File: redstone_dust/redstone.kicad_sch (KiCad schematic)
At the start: 72 parts, among them J1 1x4_Pogo, J2 1x4_Pogo, J3 1x4_Pogo, J4 1x4_Pogo, J5 1x4_Pogo, J6 1x4_Pogo, J7 1x4_Pogo, J8 1x4_Pogo, J9 2.54mm_ProgrammingPin, Q1 BC108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

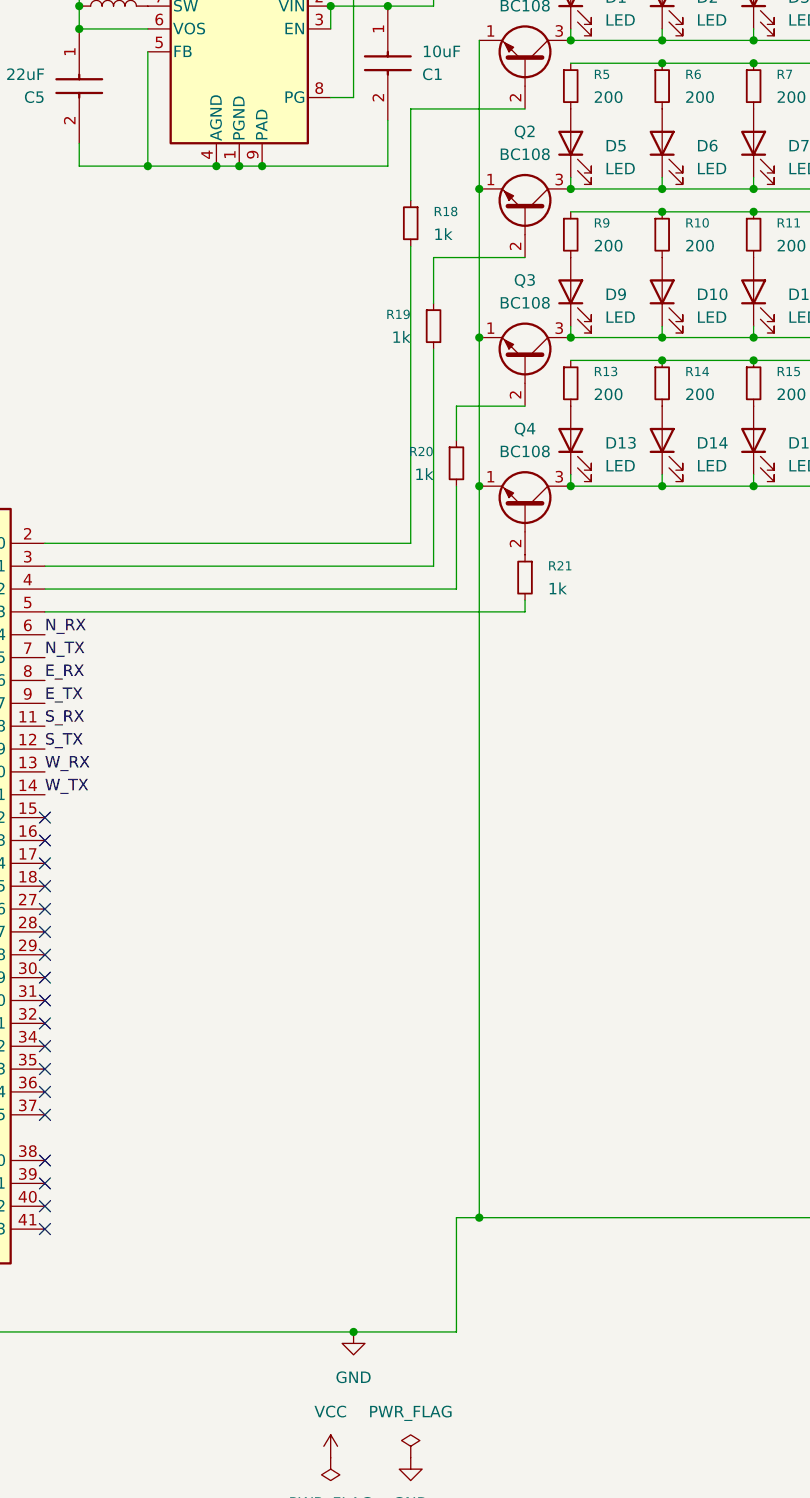
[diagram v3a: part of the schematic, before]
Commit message: add basic pcb layout, fix disconnected ground net
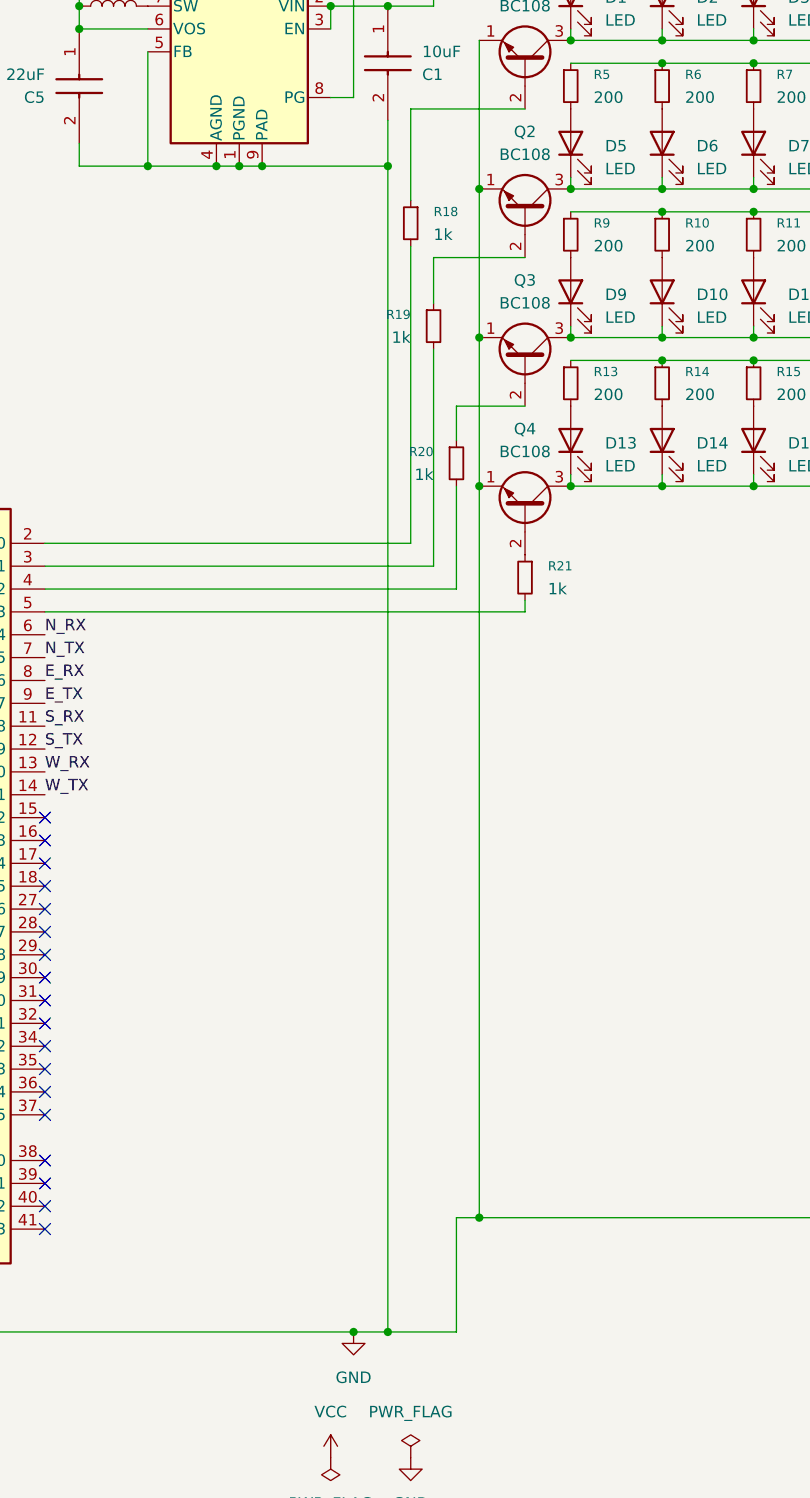
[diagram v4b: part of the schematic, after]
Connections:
- net GND: now also C1.2, C5.2, U3.1 (PGND), U3.4 (AGND), U3.5 (FB), U3.9 (PAD)
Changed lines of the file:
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@@
+	)
+	(junction
+		(at 166.37 173.99)
+		(diameter 0)
+		(color 0 0 0 1)
 	)
 	(junction
@@
 	)
 	(junction
+		(at 166.37 44.45)
+		(diameter 0)
+		(color 0 0 0 1)
+	)
+	(junction
 		(at 110.49 16.51)
 		(diameter 0)
@@
 	(wire
 		(pts
+			(xy 166.37 173.99) (xy 173.99 173.99)
+		)
+		(stroke
+			(width 0)
+			(type default)
+			(color 0 0 0 1)
+		)
+	)
+	(wire
+		(pts
 			(xy 48.26 149.86) (xy 48.26 86.36)
 		)
@@
 	(wire
 		(pts
+			(xy 166.37 44.45) (xy 166.37 173.99)
+		)
+		(stroke
+			(width 0)
+			(type default)
+			(color 0 0 0 1)
+		)
+	)
+	(wire
+		(pts
 			(xy 82.55 59.69) (xy 82.55 67.31)
 		)
@@
 	(wire
 		(pts
-			(xy 162.56 173.99) (xy 173.99 173.99)
-		)
-		(stroke
+			(xy 162.56 173.99) (xy 166.37 173.99)
+		)
+		(stroke

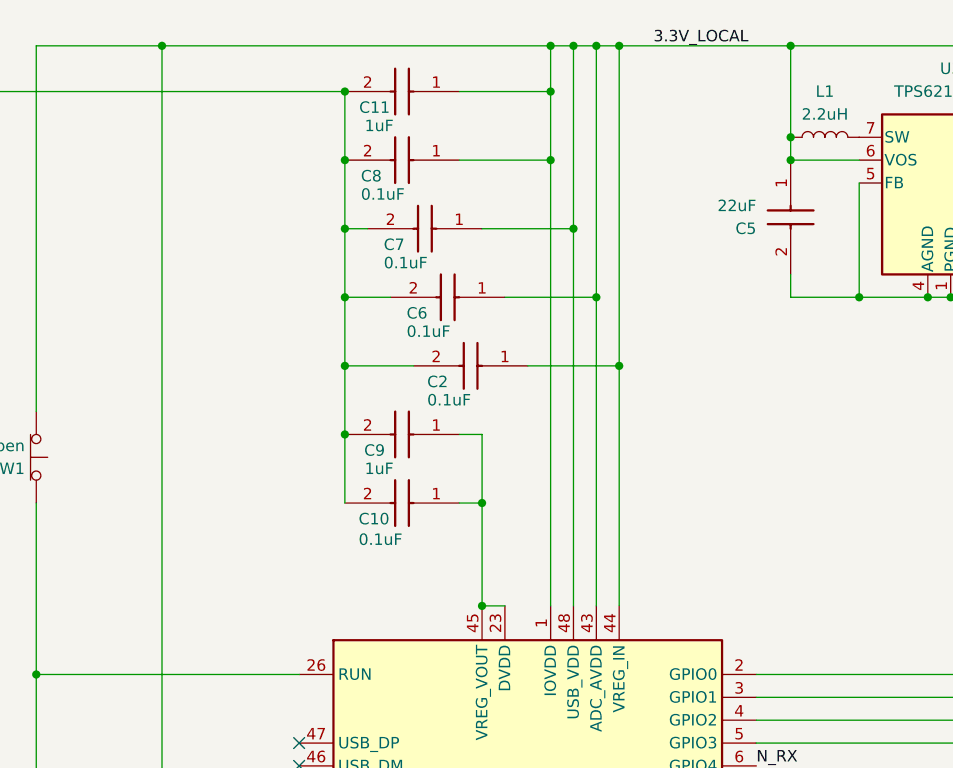
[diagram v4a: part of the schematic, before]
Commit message: remove some unecessary capacitors
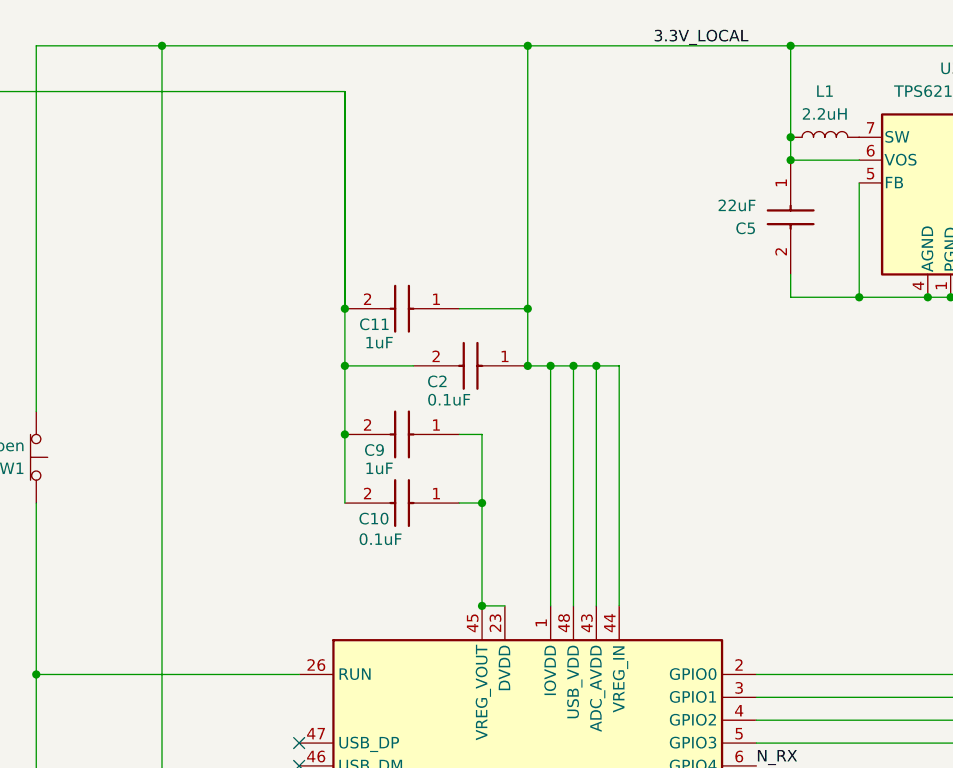
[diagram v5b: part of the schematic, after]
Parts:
- removed C6, C7, C8: 0.1uF, CAPC2012X140N, symbol SamacSys_Parts:C0805F104K1RACAUTO
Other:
- moved on the sheet: C11

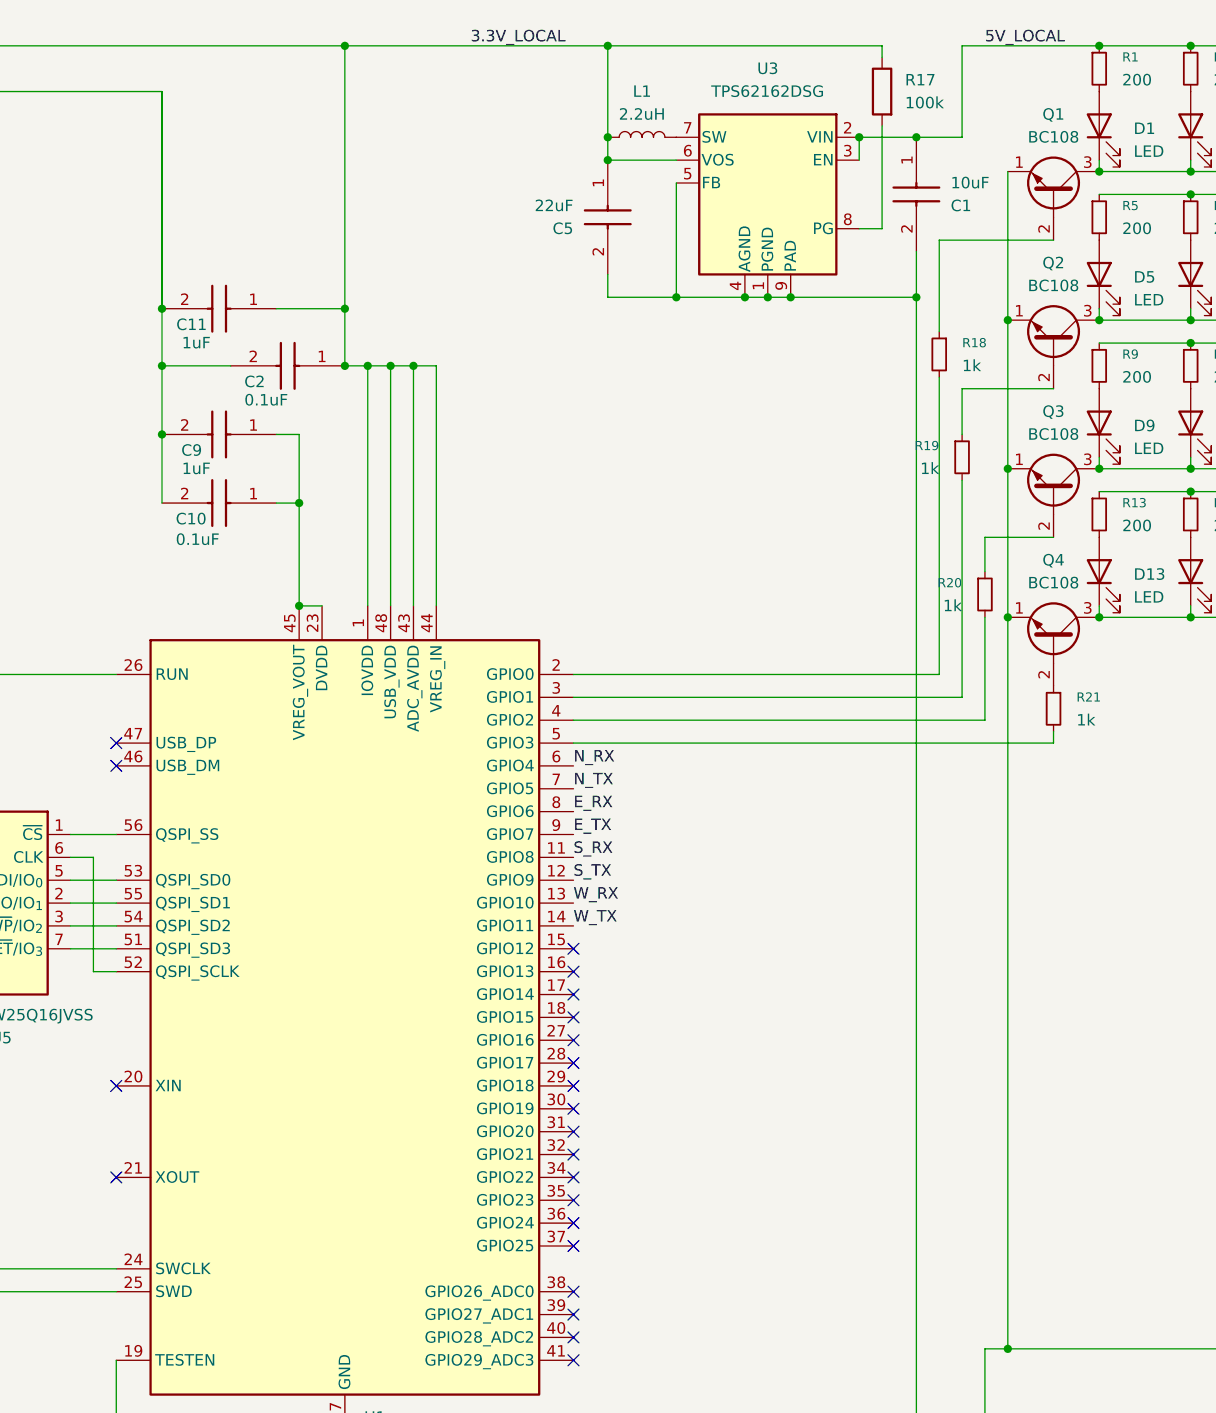
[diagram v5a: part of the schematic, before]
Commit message: redoing pcb layout with new approach
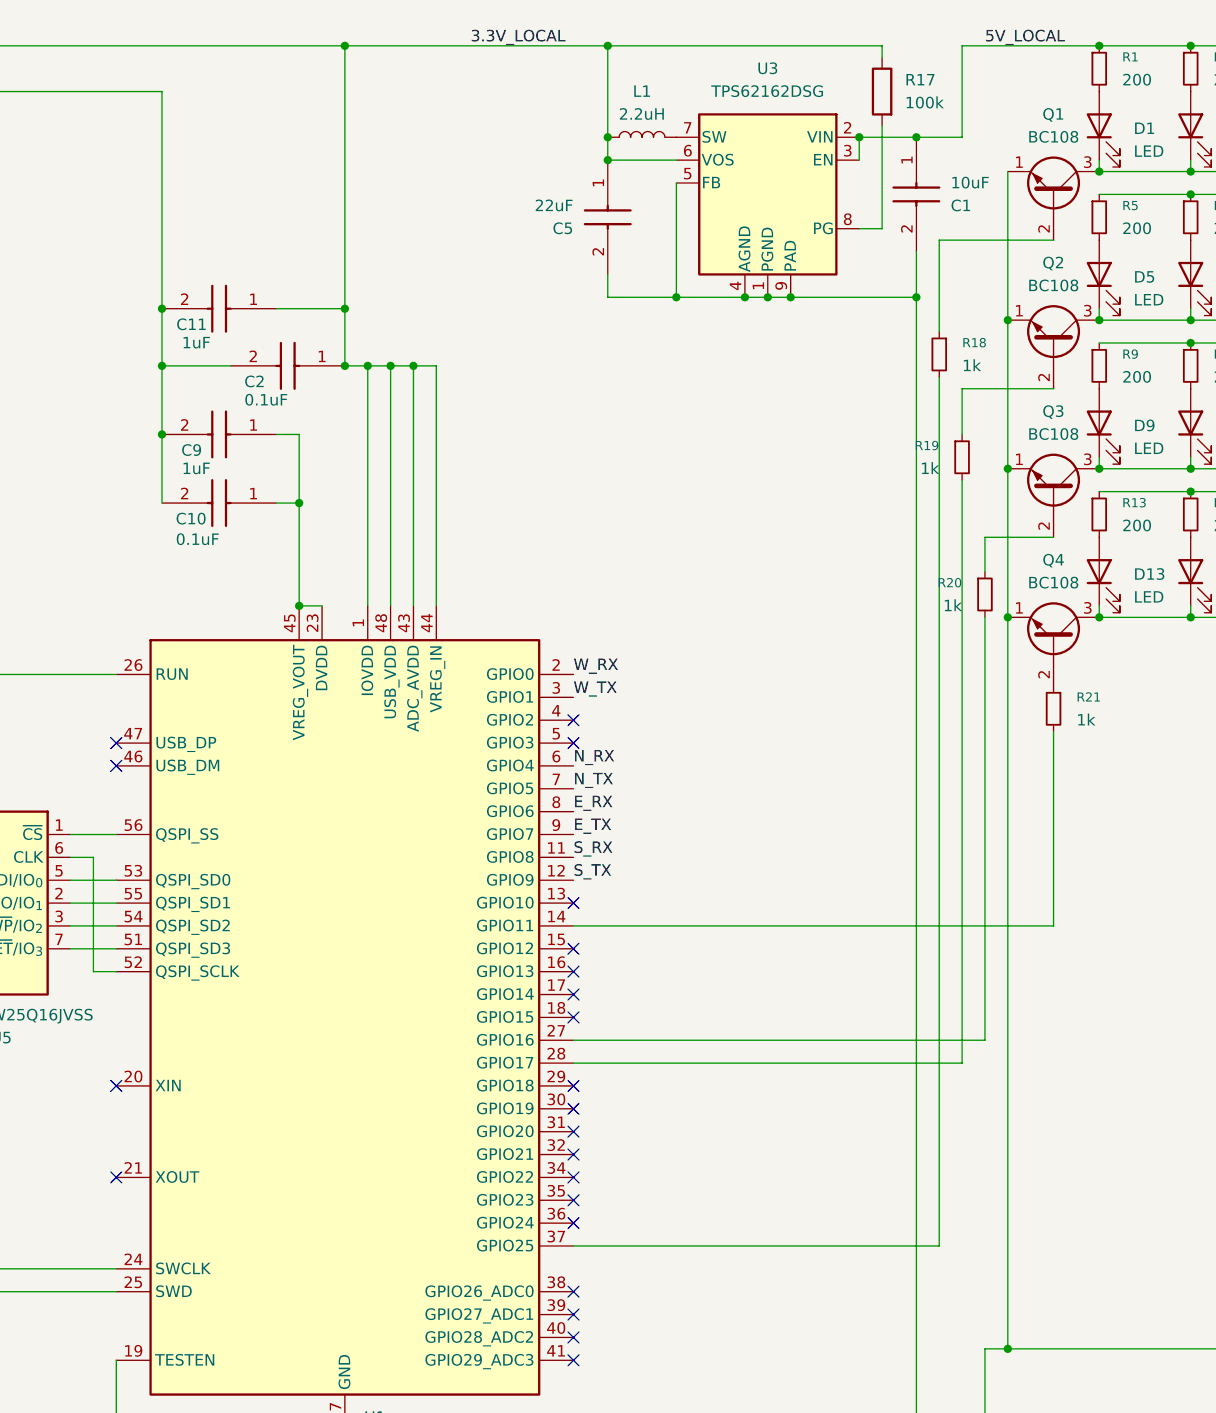
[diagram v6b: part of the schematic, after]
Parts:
- C1: footprint CAPC1005X70N -> SamacSys_Parts:CAPC1005X70N
- C10, C2, C3: footprint CAPC2012X140N -> SamacSys_Parts:CAPC2012X140N
- C11, C9: footprint CAPC0603X33N -> SamacSys_Parts:CAPC0603X33N
- C4, C5: footprint GRM18x -> SamacSys_Parts:GRM18x
- D17, D18, D20, D21: footprint SOT95P248X115-3N -> SamacSys_Parts:SOT95P248X115-3N
- D19: footprint DIOM5436X244N -> SamacSys_Parts:DIOM5436X244N
- U2: footprint RBT10W24S05_XPP_XPR -> SamacSys_Parts:RBT10W24S05_XPP_XPR
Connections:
- net W_RX: now also U1.2 (GPIO0); no longer U1.13 (GPIO10)
- net W_TX: now also U1.3 (GPIO1); no longer U1.14 (GPIO11)
- net at R18.2: now also U1.37 (GPIO25); no longer U1.2 (GPIO0)
- net at R19.2: now also U1.28 (GPIO17); no longer U1.3 (GPIO1)
- net at R20.2: now also U1.27 (GPIO16); no longer U1.4 (GPIO2)
- net at R21.2: now also U1.14 (GPIO11); no longer U1.5 (GPIO3)
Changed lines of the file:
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@@
 	)
 	(no_connect
-		(at 128.27 129.54)
+		(at 128.27 93.98)
 	)
 	(no_connect
@@
 	)
 	(no_connect
-		(at 128.27 149.86)
+		(at 128.27 111.76)
 	)
 	(no_connect
@@
 	)
 	(no_connect
-		(at 128.27 127)
+		(at 128.27 91.44)
 	)
 	(no_connect
@@
 	(wire
 		(pts
-			(xy 171.45 88.9) (xy 171.45 64.77)
+			(xy 171.45 64.77) (xy 171.45 129.54)
 		)
 		(stroke
@@
 	(wire
 		(pts
-			(xy 128.27 93.98) (xy 181.61 93.98)
+			(xy 128.27 114.3) (xy 181.61 114.3)
 		)
 		(stroke
@@
 	(wire
 		(pts
-			(xy 168.91 53.34) (xy 168.91 86.36)
-		)
-		(stroke
-			(width 0)
-			(type default)
-			(color 0 194 194 1)
-		)
-	)
-	(wire
-		(pts
 			(xy 257.81 59.69) (xy 265.43 59.69)
 		)
@@
 	(wire
 		(pts
-			(xy 128.27 91.44) (xy 173.99 91.44)
+			(xy 128.27 127) (xy 173.99 127)
 		)
 		(stroke
@@
 	(wire
 		(pts
-			(xy 181.61 93.98) (xy 181.61 92.71)
+			(xy 181.61 92.71) (xy 181.61 114.3)
 		)
 		(stroke
@@
 	(wire
 		(pts
-			(xy 128.27 88.9) (xy 171.45 88.9)
+			(xy 128.27 129.54) (xy 171.45 129.54)
 		)
 		(stroke
@@
 	(wire
 		(pts
-			(xy 173.99 80.01) (xy 173.99 91.44)
+			(xy 173.99 80.01) (xy 173.99 127)
 		)
 		(stroke
@@
 	(wire
 		(pts
-			(xy 168.91 86.36) (xy 128.27 86.36)
+			(xy 168.91 149.86) (xy 128.27 149.86)
 		)
 		(stroke
@@
 	(wire
 		(pts
-			(xy 82.55 45.72) (xy 82.55 21.59)
-		)
-		(stroke
-			(width 0)
-			(type default)
-			(color 0 0 0 1)
-		)
-	)
-	(wire
-		(pts
 			(xy 207.01 45.72) (xy 207.01 46.99)
 		)
@@
 	(wire
 		(pts
+			(xy 168.91 53.34) (xy 168.91 149.86)
+		)
+		(stroke
+			(width 0)
+			(type default)
+			(color 0 194 194 1)
+		)
+	)
+	(wire
+		(pts
 			(xy 102.87 16.51) (xy 102.87 45.72)
 		)
@@
 	)
 	(label "W_TX"
-		(at 128.27 114.3 0)
+		(at 128.27 88.9 0)
 		(effects
 			(font
@@
 	)
 	(label "W_RX"
-		(at 128.27 111.76 0)
+		(at 128.27 86.36 0)
 		(effects
 			(font
@@
 			)
 		)
-		(property "Footprint" "DIOM5436X244N"
+		(property "Footprint" "SamacSys_Parts:DIOM5436X244N"
 			(at 275.59 115.24 0)
 			(effects
@@
 			)
 		)
-		(property "Footprint" "CAPC2012X140N"
+		(property "Footprint" "SamacSys_Parts:CAPC2012X140N"
 			(at 326.06 157.48 0)
 			(effects
@@
 			)
 		)
-		(property "Footprint" "GRM18x"
+		(property "Footprint" "SamacSys_Parts:GRM18x"
 			(at 313.36 157.48 0)
 			(effects
@@
 			)
 		)
-		(property "Footprint" "CAPC0603X33N"
+		(property "Footprint" "SamacSys_Parts:CAPC0603X33N"
 			(at 86.36 155.88 0)
 			(effects
@@
 			)
 		)
-		(property "Footprint" "GRM18x"
+		(property "Footprint" "SamacSys_Parts:GRM18x"
 			(at 35.89 38.1 0)
 			(effects
@@
 			)
 		)
-		(property "Footprint" "CAPC1005X70N"
+		(property "Footprint" "SamacSys_Parts:CAPC1005X70N"
 			(at 262.56 35.56 0)
 			(effects
@@
 			)
 		)
-		(property "Footprint" "SOT95P248X115-3N"
+		(property "Footprint" "SamacSys_Parts:SOT95P248X115-3N"
 			(at 345.11 157.48 0)
 			(effects
@@
 			)
 		)
-		(property "Footprint" "CAPC2012X140N"
+		(property "Footprint" "SamacSys_Parts:CAPC2012X140N"
 			(at 86.36 163.5 0)
 			(effects
@@
 			)
 		)
-		(property "Footprint" "RBT10W24S05_XPP_XPR"
+		(property "Footprint" "SamacSys_Parts:RBT10W24S05_XPP_XPR"
 			(at 234.95 19.05 0)
 			(effects
@@
 			)
 		)
-		(property "Footprint" "CAPC0603X33N"
+		(property "Footprint" "SamacSys_Parts:CAPC0603X33N"
 			(at 86.36 141.91 0)
 			(effects
@@
 			)
 		)
-		(property "Footprint" "SOT95P248X115-3N"
+		(property "Footprint" "SamacSys_Parts:SOT95P248X115-3N"
 			(at 345.11 91.44 0)
 			(effects
@@
 			)
 		)
-		(property "Footprint" "SOT95P248X115-3N"
+		(property "Footprint" "SamacSys_Parts:SOT95P248X115-3N"
 			(at 345.11 58.42 0)
 			(effects
@@
 			)
 		)
-		(property "Footprint" "CAPC2012X140N"
+		(property "Footprint" "SamacSys_Parts:CAPC2012X140N"
 			(at 93.98 148.26 0)
 			(effects
@@
 			)
 		)
-		(property "Footprint" "SOT95P248X115-3N"
+		(property "Footprint" "SamacSys_Parts:SOT95P248X115-3N"
 			(at 345.11 124.46 0)
 			(effects

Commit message: connect more traces, progress is well
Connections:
- net E_RX: now also U1.31 (GPIO20); no longer U1.8 (GPIO6)
- net E_TX: now also U1.32 (GPIO21); no longer U1.9 (GPIO7)
- net N_RX: now also U1.36 (GPIO24); no longer U1.6 (GPIO4)
- net N_TX: now also U1.37 (GPIO25); no longer U1.7 (GPIO5)
- net at R18.2: now also U1.35 (GPIO23); no longer U1.37 (GPIO25)
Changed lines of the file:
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@@
 	)
 	(no_connect
-		(at 128.27 147.32)
+		(at 128.27 99.06)
 	)
 	(no_connect
-		(at 128.27 137.16)
+		(at 128.27 101.6)
 	)
 	(no_connect
@@
 	)
 	(no_connect
-		(at 128.27 144.78)
+		(at 128.27 96.52)
 	)
 	(no_connect
@@
 	)
 	(no_connect
-		(at 128.27 139.7)
+		(at 128.27 104.14)
 	)
 	(wire
@@
 	(wire
 		(pts
-			(xy 168.91 149.86) (xy 128.27 149.86)
+			(xy 168.91 144.78) (xy 128.27 144.78)
 		)
 		(stroke
@@
 	(wire
 		(pts
-			(xy 168.91 53.34) (xy 168.91 149.86)
+			(xy 168.91 53.34) (xy 168.91 144.78)
 		)
 		(stroke
@@
 	)
 	(label "N_RX"
-		(at 128.27 96.52 0)
+		(at 128.27 147.32 0)
 		(effects
 			(font
@@
 	)
 	(label "N_TX"
-		(at 128.27 99.06 0)
+		(at 128.27 149.86 0)
 		(effects
 			(font
@@
 	)
 	(label "E_RX"
-		(at 128.27 101.6 0)
+		(at 128.27 137.16 0)
 		(effects
 			(font
@@
 	)
 	(label "E_TX"
-		(at 128.27 104.14 0)
+		(at 128.27 139.7 0)
 		(effects
 			(font
